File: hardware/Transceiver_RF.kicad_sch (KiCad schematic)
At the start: 38 parts, among them J12 Conn_Coaxial, J5 Conn_Coaxial, J6 Conn_Coaxial, J7 Conn_Coaxial, J8 Conn_Coaxial, J9 Conn_Coaxial, U12 Si513A_2.5x3.2mm, U3 AD9361

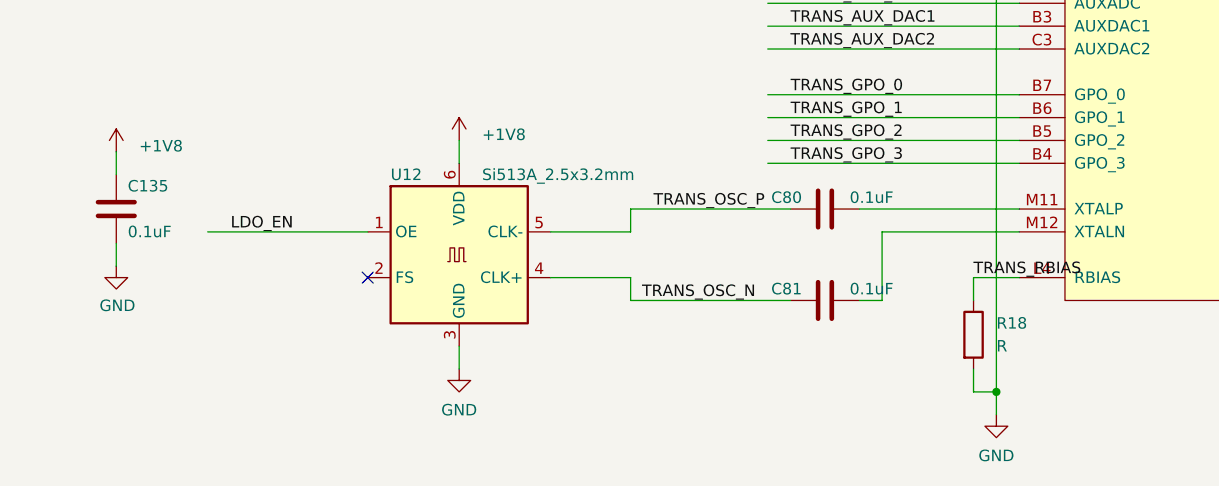
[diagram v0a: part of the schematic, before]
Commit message: add sdio level shift ciruit
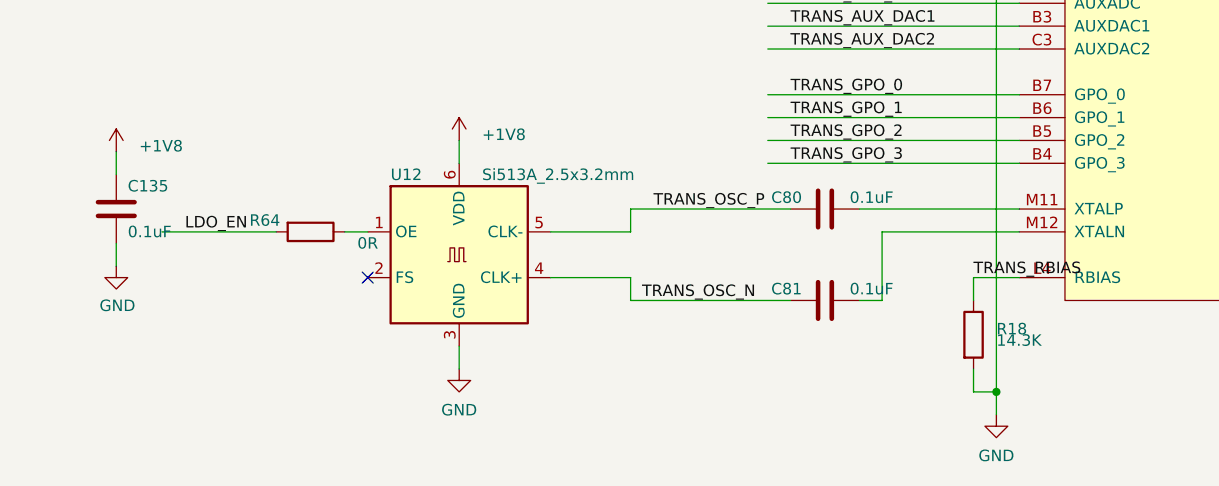
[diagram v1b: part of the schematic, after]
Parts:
- added R64: 0R, Resistor_SMD:R_0201_0603Metric, symbol Device:R
- R18: value R -> 14.3K
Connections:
- net LDO_EN: now also R64.2; no longer U12.1 (OE)
- new net: R64.1, U12.1 (OE)
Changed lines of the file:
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@@
-(kicad_sch (version 20220104) (generator eeschema)
+(kicad_sch (version 20220126) (generator eeschema)
   (paper "A3")
   (junction (at 217.17 54.61) (diameter 0) (color 0 0 0 0)
@@
     (stroke (width 0) (type default))
   )
-  (wire (pts (xy 124.46 223.52) (xy 142.24 223.52))
-    (stroke (width 0) (type default))
-  )
   (wire (pts (xy 74.93 125.73) (xy 100.33 125.73))
     (stroke (width 0) (type default))
@@
     (stroke (width 0) (type default))
   )
+  (wire (pts (xy 139.7 223.52) (xy 142.24 223.52))
+    (stroke (width 0) (type default))
+  )
   (wire (pts (xy 212.09 167.64) (xy 214.63 167.64))
     (stroke (width 0) (type default))
@@
   )
   (wire (pts (xy 209.55 238.76) (xy 209.55 241.3))
+    (stroke (width 0) (type default))
+  )
+  (wire (pts (xy 119.38 223.52) (xy 132.08 223.52))
     (stroke (width 0) (type default))
   )
@@
     (effects (font (size 1.27 1.27)) (justify left bottom))
   )
-  (label "LDO_EN" (at 127 223.52 0) (fields_autoplaced)
+  (label "LDO_EN" (at 121.92 223.52 0) (fields_autoplaced)
     (effects (font (size 1.27 1.27)) (justify left bottom))
   )
@@
     )
     (property "Datasheet" "~" (id 3) (at 195.58 116.84 0)
+      (effects (font (size 1.27 1.27)) hide)
+    )
+    (pin "1")
+    (pin "2")
+  )
+  (symbol (lib_id "Device:R") (at 135.89 223.52 270) (unit 1)
+    (in_bom yes) (on_board yes)
+    (property "Reference" "R64" (id 0) (at 130.81 222.25 90)
+      (effects (font (size 1.27 1.27)))
+    )
+    (property "Value" "0R" (id 1) (at 142.24 224.79 90)
+      (effects (font (size 1.27 1.27)))
+    )
+    (property "Footprint" "Resistor_SMD:R_0201_0603Metric" (id 2) (at 135.89 221.742 90)
+      (effects (font (size 1.27 1.27)) hide)
+    )
+    (property "Datasheet" "~" (id 3) (at 135.89 223.52 0)
       (effects (font (size 1.27 1.27)) hide)
     )
@@
   (symbol (lib_id "Device:R") (at 209.55 234.95 0) (unit 1)
     (in_bom yes) (on_board yes) (fields_autoplaced)
-    (property "Reference" "R18" (id 0) (at 212.09 233.6799 0)
-      (effects (font (size 1.27 1.27)) (justify left))
-    )
-    (property "Value" "R" (id 1) (at 212.09 236.2199 0)
-      (effects (font (size 1.27 1.27)) (justify left))
-    )
+    (property "Reference" "R18" (id 0) (at 212.09 234.315 0)
+      (effects (font (size 1.27 1.27)) (justify left))
+    )
+    (property "Value" "14.3K" (id 1) (at 212.09 235.585 0)
+      (effects (font (size 1.27 1.27)) (justify left))
+    )

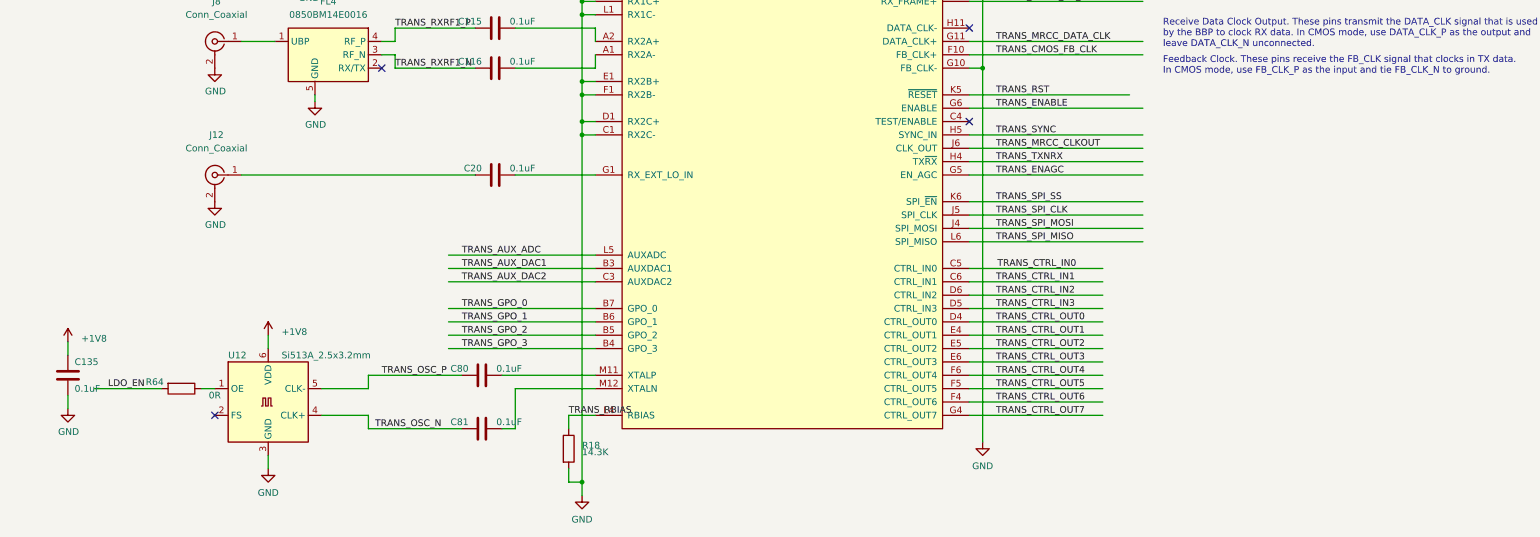
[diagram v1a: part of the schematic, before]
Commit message: Add PS I2C pullup resistor
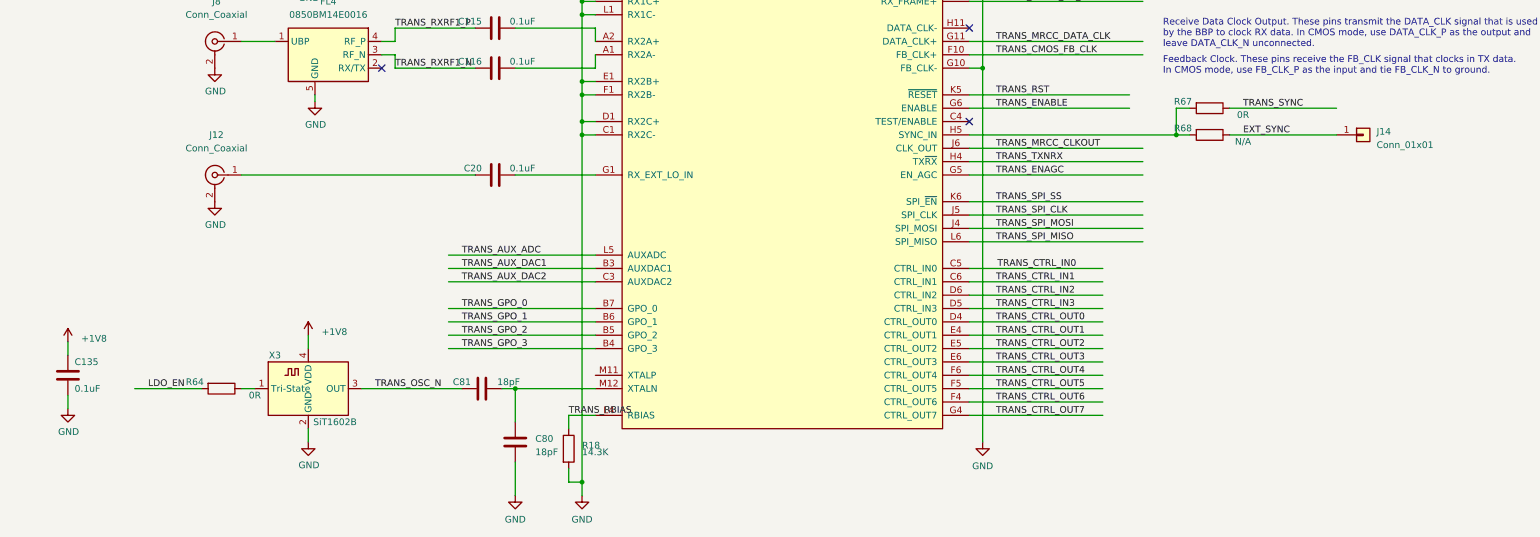
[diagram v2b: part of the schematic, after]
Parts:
- removed U12: Si513A_2.5x3.2mm, Oscillator:Oscillator_SMD_Silicon_Labs_LGA-6_2.5x3.2mm_P1.25mm, symbol Oscillato_Local:Si513A_2.5x3.2mm
- added J14: Conn_01x01, Connector_PinHeader_2.54mm:PinHeader_1x01_P2.54mm_Vertical, symbol Connector_Generic:Conn_01x01
- added R67: 0R, Resistor_SMD:R_0201_0603Metric, symbol Device:R
- added R68: N/A, Resistor_SMD:R_0201_0603Metric, symbol Device:R
- added X3: SiT1602B, Oscillator:Oscillator_SMD_ECS_2520MV-xxx-xx-4Pin_2.5x2.0mm, symbol 7z010_ddr:ECS-2520MV-xxx-xx
- C80, C81: value 0.1uF -> 18pF
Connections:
- net TRANS_OSC_P is gone; now on net GND: C80.1
- net +1V8: now also X3.4 (VDD)
- net GND: now also X3.2 (GND)
- net TRANS_OSC_N: now also X3.3 (OUT)
- net TRANS_SYNC: now also R67.1; no longer U3.H5 (SYNC_IN)
- net at R64.1: now also X3.1 (Tri-State)
- net at C80.2: now also C81.2, U3.M12 (XTALN); no longer U3.M11 (XTALP)
- new net: R67.2, R68.2, U3.H5 (SYNC_IN)
- new net EXT_SYNC: J14.1 (Pin_1), R68.1
- no-connect marks 9 -> 8
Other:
- moved on the sheet: C80, C81, R64
